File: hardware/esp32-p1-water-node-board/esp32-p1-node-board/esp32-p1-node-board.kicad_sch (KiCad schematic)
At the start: 22 parts, among them J1 RJ11-6, J2 Conn_01x03, Q1 BSS138, Q2 BSS138, Q3 BSS138

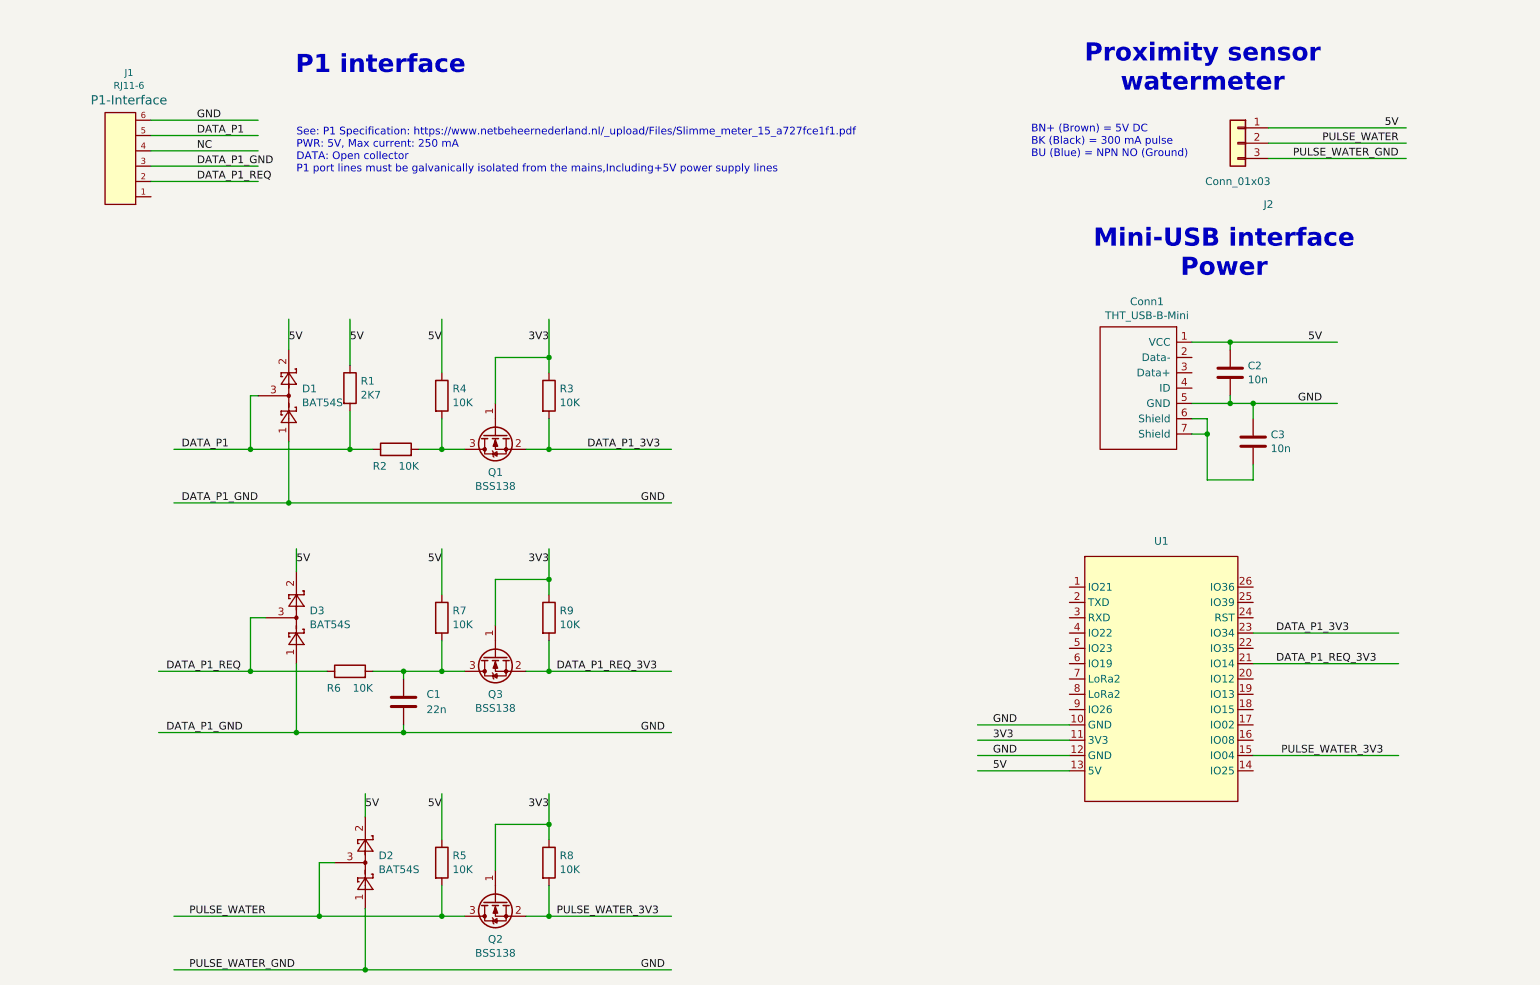
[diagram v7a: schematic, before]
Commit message: Updated PCB to version 0.5
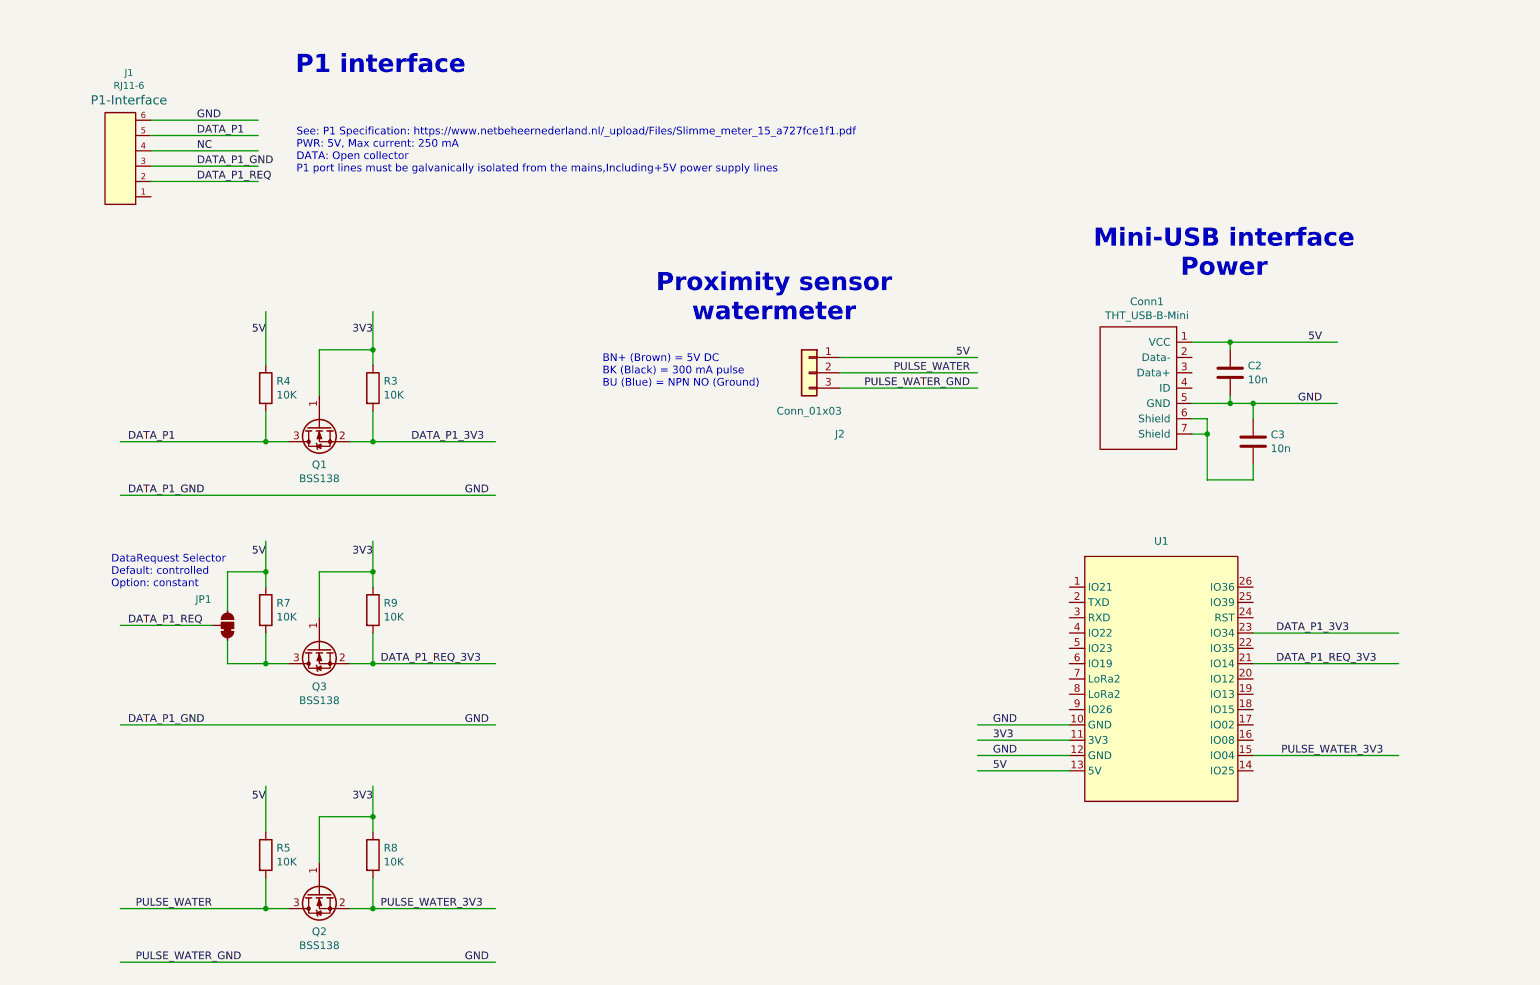
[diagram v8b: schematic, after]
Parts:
- removed C1: 22n, Capacitor_SMD:C_1206_3216Metric, symbol Device:C
- removed D1, D2, D3: BAT54S, Package_TO_SOT_SMD:SOT-23, symbol esp32-p1-node-board-rescue:BAT54S-Diode
- removed R1: 2K7, Resistor_SMD:R_1206_3216Metric, symbol Device:R
- removed R2, R6: 10K, Resistor_SMD:R_1206_3216Metric, symbol Device:R
- added JP1: ~, Sparkfun Jumpers:Jumper_3_NC-1_Trace_NoSilk, symbol SparkFun-Jumper:SolderJumper_3_Bridged12_No_Silk
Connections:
- net 5V: now also JP1.2 (C)
- net DATA_P1: now also Q1.3 (D), R4.2
- net DATA_P1_REQ: now also JP1.2 (C)
- net at Q3.3 (D), R7.2: now also JP1.1 (A)
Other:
- note added: "DataRequest Selector Default: controlled Option: constant"
- moved on the sheet: J2, Q1, Q2, Q3, R3, R4, R5, R7, R8, R9
